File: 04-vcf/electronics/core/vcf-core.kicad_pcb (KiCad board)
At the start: 2 copper layers, 58 x 65 mm, 89 parts, among them J1 Conn_01x06, J2 Conn_02x04_Counter_Clockwise, J3 Conn_02x02_Counter_Clockwise, J4 S1711-46R, J5 S1711-46R, J6 Conn_02x03_Odd_Even, J7 Conn_01x02, J8 Conn_02x05_Odd_Even, Q1 BC847BS, U1 TL072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

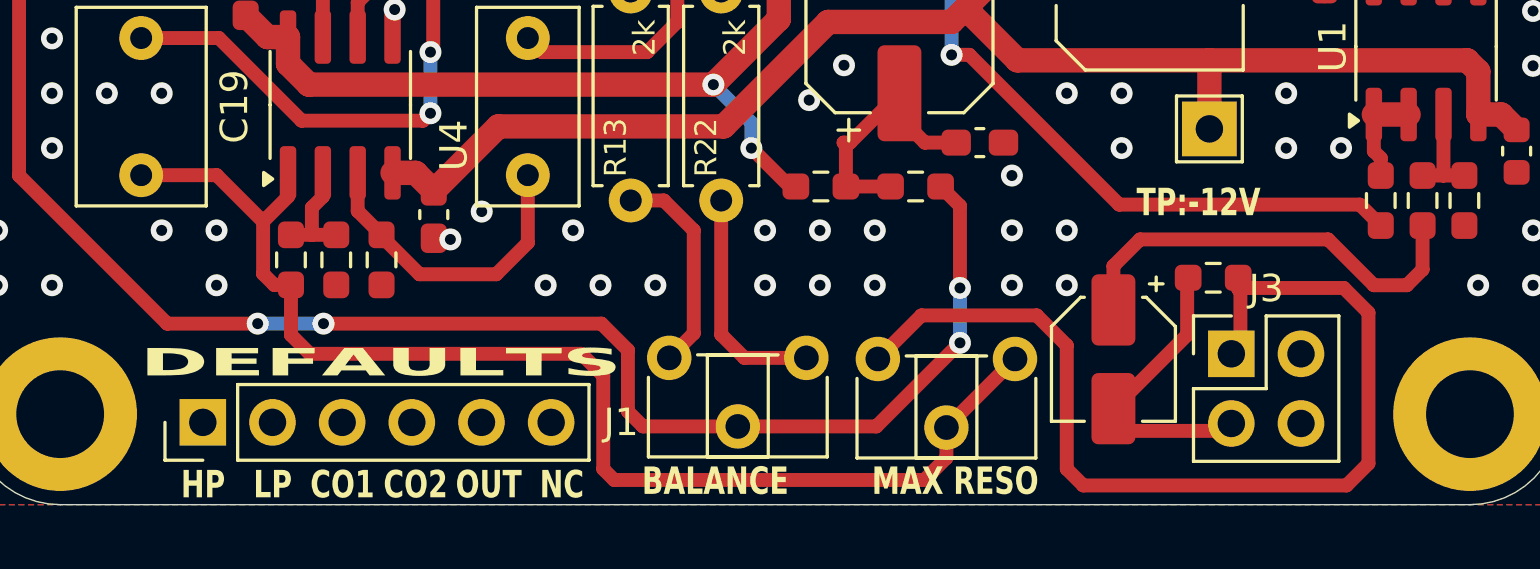
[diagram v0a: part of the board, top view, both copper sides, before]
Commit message: Designed UI schematics for VCF
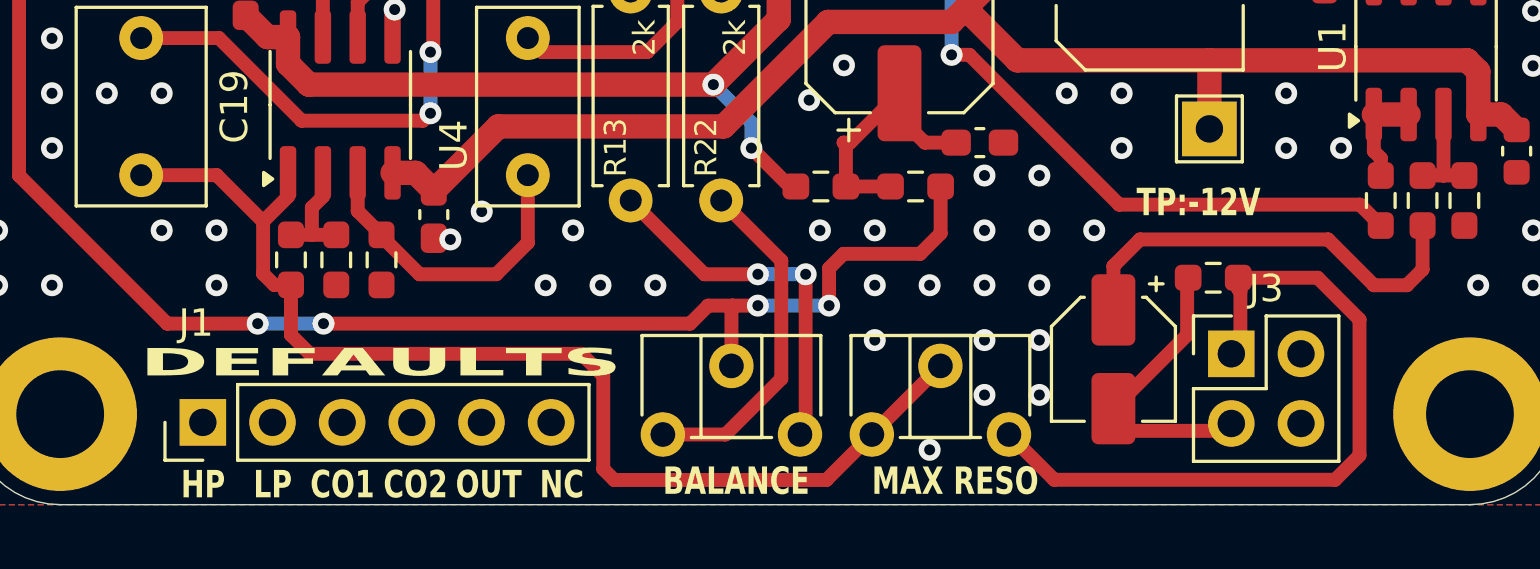
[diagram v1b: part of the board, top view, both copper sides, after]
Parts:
- moved RV_BALANCE1 5.93 mm to (149.3, 151.4), turned to 90 degrees
- moved RV_MAX_RESO1 5.90 mm to (156.9, 151.4), turned to 90 degrees
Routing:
- net RESO_OUT: track 38.1 -> 27.1 mm
- net Net-(R13-Pad1): track 7.77 -> 13.4 mm, vias 0 -> 2
- net Net-(C11-Pad1): track 56.1 -> 51.4 mm
- net Net-(R22-Pad1): track 8.35 -> 12.6 mm
- net Net-(C19-Pad2): track 45.3 -> 41.8 mm
- net GND: vias 172 -> 178

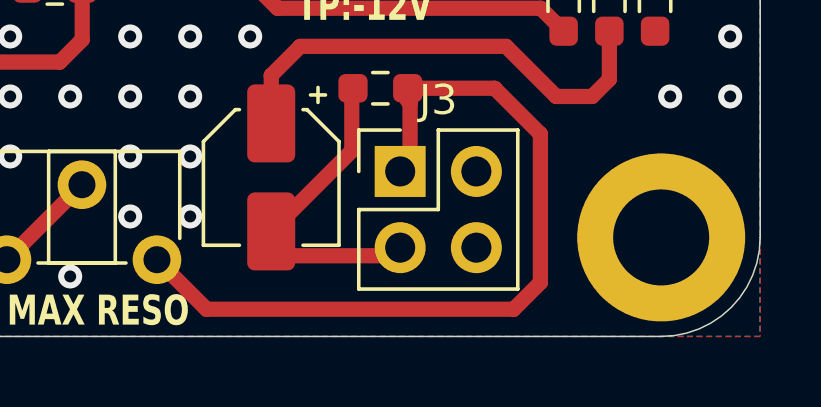
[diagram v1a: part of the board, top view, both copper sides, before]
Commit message: Designed VCF UI board pre-check
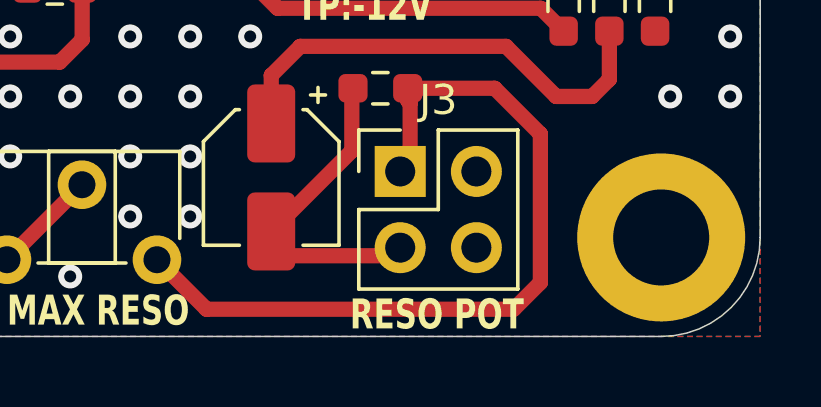
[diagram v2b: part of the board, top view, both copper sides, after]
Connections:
- net RESO_IN renamed RESO_VALUE
- net RESO_OUT renamed RESO_MAX
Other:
- board text added: "RESO POT"
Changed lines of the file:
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@@
 	(net 18 "Net-(C19-Pad2)")
 	(net 19 "Net-(C20-Pad1)")
-	(net 20 "RESO_IN")
+	(net 20 "RESO_VALUE")
 	(net 21 "Net-(D1-K)")
 	(net 22 "Net-(D1-A)")
@@
 	(net 37 "OUT")
 	(net 38 "LP")
-	(net 39 "RESO_OUT")
+	(net 39 "RESO_MAX")
 	(net 40 "Net-(Q1A-B1)")
 	(net 41 "Net-(Q1A-E1)")
@@
 			(layers "F.Cu" "F.Mask" "F.Paste")
 			(roundrect_rratio 0.25)
-			(net 39 "RESO_OUT")
+			(net 39 "RESO_MAX")
 			(pintype "passive")
 		)
@@
 			(layers "F.Cu" "F.Mask" "F.Paste")
 			(roundrect_rratio 0.25)
-			(net 20 "RESO_IN")
+			(net 20 "RESO_VALUE")
 			(pintype "passive")
 		)
@@
 		(property ki_fp_filters "Connector*:*_2x??_*")
 		(sheetname "/")
-		(sheetfile "vcf.kicad_sch")
+		(sheetfile "vcf-core.kicad_sch")
 		(attr through_hole)
 		(fp_line
@@
 		(property ki_fp_filters "MountingHole*")
 		(sheetname "/")
-		(sheetfile "vcf.kicad_sch")
+		(sheetfile "vcf-core.kicad_sch")
 		(attr exclude_from_pos_files exclude_from_bom)
 		(fp_circle
@@
 		(property ki_fp_filters "Connector*:*_1x??_*")
 		(sheetname "/")
-		(sheetfile "vcf.kicad_sch")
+		(sheetfile "vcf-core.kicad_sch")
 		(attr through_hole)
 		(fp_line
@@
 		(property ki_fp_filters "MountingHole*")
 		(sheetname "/")
-		(sheetfile "vcf.kicad_sch")
+		(sheetfile "vcf-core.kicad_sch")
 		(attr exclude_from_pos_files exclude_from_bom)
 		(fp_circle
@@
 	)
 	(footprint "Connector_PinHeader_2.54mm:PinHeader_2x02_P2.54mm_Vertical"
+		(locked yes)
 		(layer "F.Cu")
 		(at 170 148.5)
@@
 		(property ki_fp_filters "Connector*:*_2x??_*")
 		(sheetname "/")
-		(sheetfile "vcf.kicad_sch")
+		(sheetfile "vcf-core.kicad_sch")
 		(attr through_hole)
 		(fp_line
@@
 			(layers "*.Cu" "*.Mask")
 			(remove_unused_layers no)
-			(net 39 "RESO_OUT")
+			(net 39 "RESO_MAX")
 			(pinfunction "Pin_1")
 			(pintype "passive")
@@
 			(layers "*.Cu" "*.Mask")
 			(remove_unused_layers no)
-			(net 20 "RESO_IN")
+			(net 20 "RESO_VALUE")
 			(pinfunction "Pin_3")
 			(pintype "passive")
@@
 		(property ki_fp_filters "MountingHole*")
 		(sheetname "/")
-		(sheetfile "vcf.kicad_sch")
+		(sheetfile "vcf-core.kicad_sch")
 		(attr exclude_from_pos_files exclude_from_bom)
 		(fp_circle
@@
 		(property ki_fp_filters "MountingHole*")
 		(sheetname "/")
-		(sheetfile "vcf.kicad_sch")
+		(sheetfile "vcf-core.kicad_sch")
 		(attr exclude_from_pos_files exclude_from_bom)
 		(fp_circle
@@
 			(layers "*.Cu" "*.Mask")
 			(remove_unused_layers no)
-			(net 39 "RESO_OUT")
+			(net 39 "RESO_MAX")
 			(pinfunction "3")
 			(pintype "passive")
@@
 			(layers "F.Cu" "F.Mask" "F.Paste")
 			(roundrect_rratio 0.15625)
-			(net 20 "RESO_IN")
+			(net 20 "RESO_VALUE")
 			(pintype "passive")
 		)
@@
 		)
 	)
+	(gr_text "RESO POT"
+		(at 168.323 153.855 0)
+		(layer "F.SilkS")
+		(effects
+			(font
+				(size 1 0.75)
+				(thickness 0.15)
+				(bold yes)
+			)
+			(justify left bottom)
+		)
+	)

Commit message: Added production files to VCF core
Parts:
- C1, C15, C16, C2, C3, C4, C5, C6, C7: footprint Capacitor_SMD:C_0603_1608Metric_Pad1.08x0.95mm_HandSolder -> Capacitor_SMD:C_0603_1608Metric

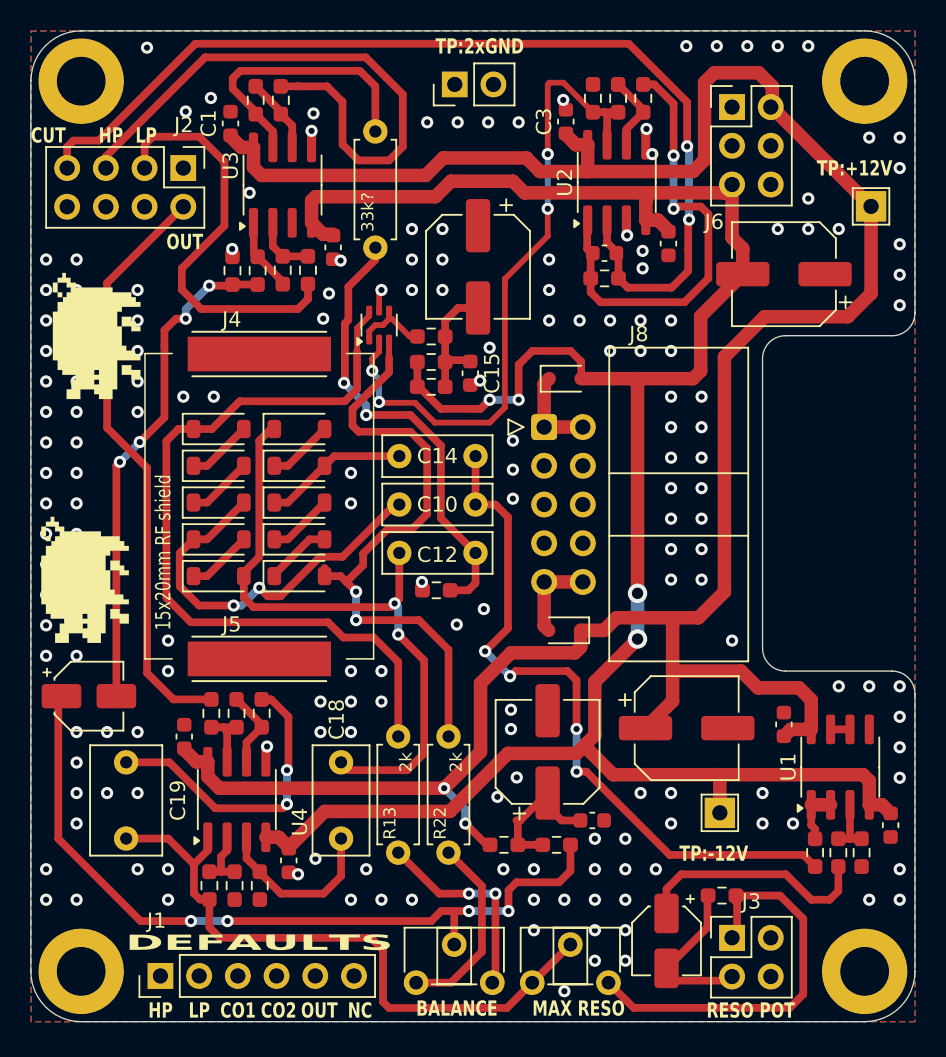
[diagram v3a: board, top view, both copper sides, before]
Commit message: V0.1 VCF PCB checked and ready for prod
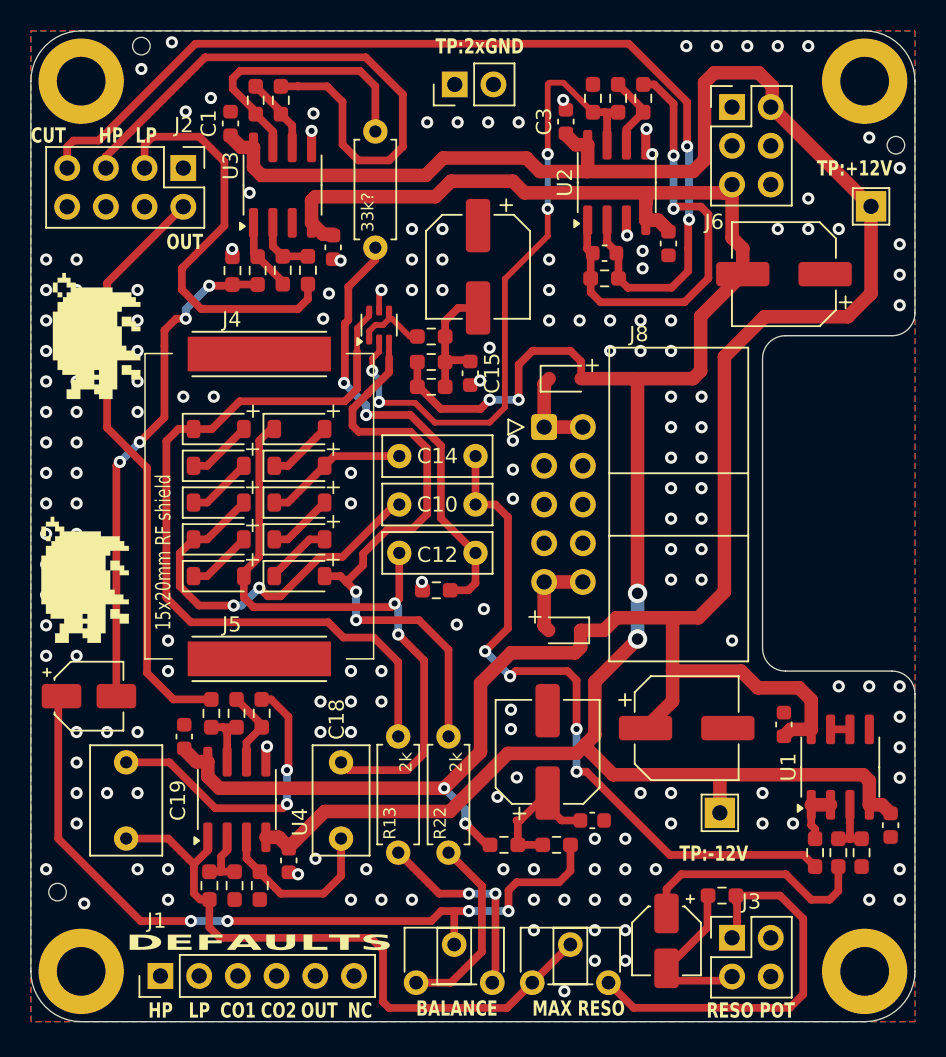
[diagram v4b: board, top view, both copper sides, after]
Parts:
- added REF**: ToolingHole_1.152mm, MountingHole:ToolingHole_1.152mm, F.Cu at (125.8, 145.5)
- added REF**: ToolingHole_1.152mm, MountingHole:ToolingHole_1.152mm, F.Cu at (180.8, 96.5)
- added REF**: ToolingHole_1.152mm, MountingHole:ToolingHole_1.152mm, F.Cu at (131.2, 90.0)
- C11: footprint Capacitor_SMD:CP_Elec_4x5.4 -> Capacitor_SMD:CP_Elec_4x5.7
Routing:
- net Net-(D10-A): track 41.5 -> 41.0 mm
- net GND: vias 178 -> 177
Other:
- board text added: "+"
